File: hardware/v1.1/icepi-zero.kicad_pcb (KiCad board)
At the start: 4 copper layers, 65 x 30 mm, 144 parts, among them J1 Conn_02x20_Counter_Clockwise, J2 HDMI_C_1.3, J3 USB_C_Receptacle_USB2.0_14P, J4 USB_C_Receptacle_USB2.0_14P, J5 USB_C_Receptacle_USB2.0_14P, J6 Micro_SD_Card_Det2, SW1 SW_Push, SW2 SW_Push, U1 ECP5U_25F_CABGA256, U10 W9825G6KH, U11 W25Q128JVS, U2 TLV62569DBV, U3 TLV62569DBV, U4 TLV62569DBV, U5 PCA9306DC1, U6 FT231XQ, U7 TPD2EUSB30A, U8 TPD2EUSB30A, U9 TPD2EUSB30A, Y1 SITxxxxxx-1x-33E-50.000000

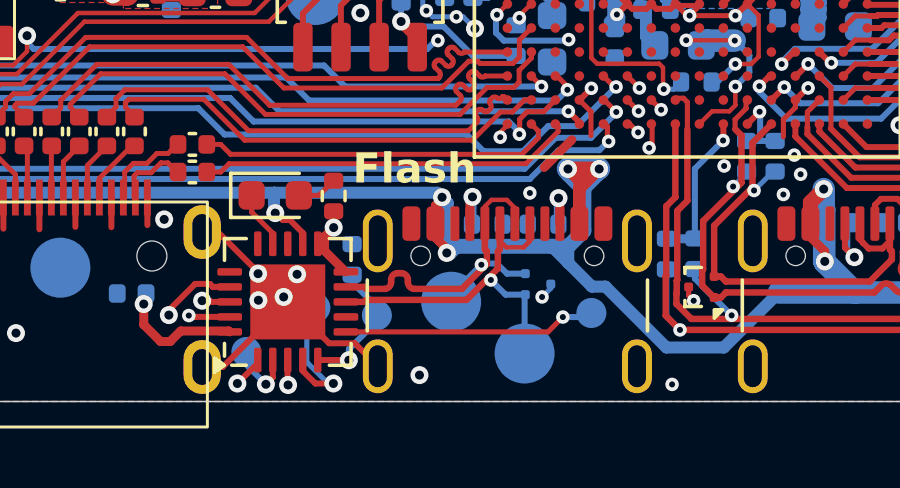
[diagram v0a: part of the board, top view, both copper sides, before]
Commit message: Fix wrong dates on shematic and pcb sheet
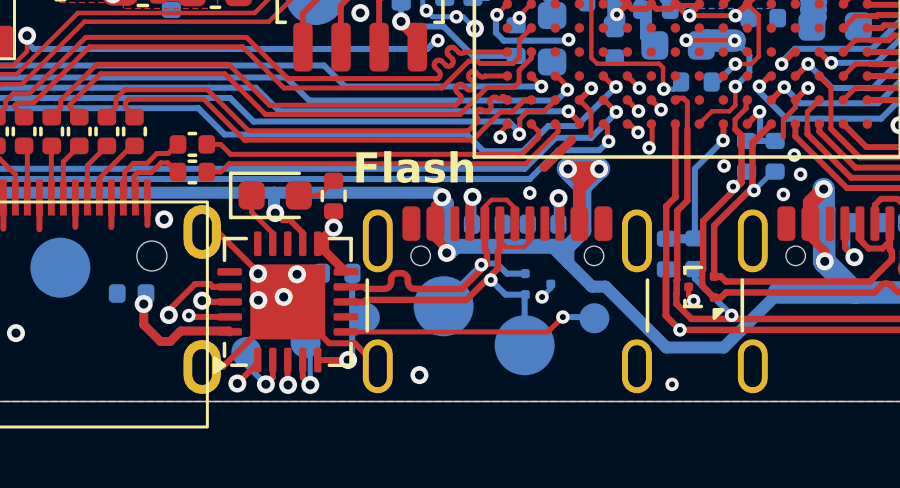
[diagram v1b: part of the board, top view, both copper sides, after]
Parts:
- moved TP9 1.22 mm to (137.3, 118.0)
- moved R25 0.68 mm to (138.3, 115.7), turned to 180 degrees
- moved TP12 0.41 mm to (139.2, 117.2)
- moved TP7 0.29 mm to (141.9, 116.8)
- moved TP8 0.28 mm to (144.6, 118.1)
- moved TP11 0.20 mm to (146.9, 117.2)
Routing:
- net JTAG_TCK: track 35.9 -> 33.9 mm

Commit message: Update pcb pic on readme
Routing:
- net GND: track 83.6 -> 89.4 mm
- net +5V: track 187.1 -> 185.6 mm
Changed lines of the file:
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@@
 	)
 	(segment
+		(start 146.786 111.378811)
+		(end 147.499999 112.09281)
+		(width 0.17)
+		(layer "F.Cu")
+		(net 38)
+	)
+	(segment
 		(start 130 100.25)
 		(end 129.54 100.71)
@@
 	)
 	(segment
+		(start 147.499999 112.09281)
+		(end 147.499999 113.770001)
+		(width 0.17)
+		(layer "F.Cu")
+		(net 38)
+	)
+	(segment
 		(start 135.803788 98.2425)
 		(end 135.3025 98.2425)
@@
 	)
 	(segment
+		(start 146.786 110.336)
+		(end 146.786 111.378811)
+		(width 0.17)
+		(layer "F.Cu")
+		(net 38)
+	)
+	(segment
 		(start 148.8 105.991141)
 		(end 149.208767 106.399908)
@@
 	)
 	(segment
+		(start 147.499999 113.770001)
+		(end 147.2 114.07)
+		(width 0.17)
+		(layer "F.Cu")
+		(net 38)
+	)
+	(segment
 		(start 150.4 110.75)
 		(end 150.824 110.326)
@@
 	)
 	(segment
+		(start 146.4 109.95)
+		(end 146.786 110.336)
+		(width 0.17)
+		(layer "F.Cu")
+		(net 38)
+	)
+	(segment
 		(start 149.92763 106.323234)
 		(end 149.950864 106.3)
@@
 	)
 	(segment
-		(start 146.786 110.336)
-		(end 146.786 111.139)
-		(width 0.17)
-		(layer "F.Cu")
-		(net 38)
-	)
-	(segment
 		(start 148.371717 103.979252)
 		(end 148.400001 103.950968)
@@
 	)
 	(segment
-		(start 146.4 109.95)
-		(end 146.786 110.336)
-		(width 0.17)
-		(layer "F.Cu")
-		(net 38)
-	)
-	(segment
 		(start 145.176 105.574)
 		(end 145.774 105.574)
@@
 	)
 	(segment
+		(start 141.1465 106.1735)
+		(end 139.9765 106.1735)
+		(width 0.165)
+		(layer "B.Cu")
+		(net 38)
+	)
+	(segment
 		(start 152.066 108.456)
 		(end 151.58 107.97)
@@
 	)
 	(segment
+		(start 139.9765 106.1735)
+		(end 139.1 107.05)
+		(width 0.165)
+		(layer "B.Cu")
+		(net 38)
+	)
+	(segment
 		(start 152.13 103.76)
 		(end 151.21 103.76)
@@
 	)
 	(segment
+		(start 141.18 106.14)
+		(end 141.1465 106.1735)
+		(width 0.165)
+		(layer "B.Cu")
+		(net 38)
+	)
+	(segment
 		(start 149.23 106.37)
 		(end 149.58 106.02)
@@
 	)
 	(segment
+		(start 146.85 112.46)
+		(end 146.4 112.91)
+		(width 0.4)
+		(layer "F.Cu")
+		(net 48)
+	)
+	(segment
 		(start 136.749581 99.675)
 		(end 136.731258 99.693323)
@@
 	)
 	(segment
+		(start 146.4 112.91)
+		(end 146.4 114.07)
+		(width 0.4)
+		(layer "F.Cu")
+		(net 48)
+	)
+	(segment
 		(start 131.85 100.2)
 		(end 131.97 100.2)
@@
 	)
 	(segment
-		(start 146.4 114.07)
-		(end 146.4 112.91)
-		(width 0.4)
-		(layer "F.Cu")
-		(net 48)
-	)
-	(segment
 		(start 171.4 114.608281)
 		(end 170.96 115.048281)
@@
 	)
 	(segment
+		(start 146.85 112.25)
+		(end 146.85 112.46)
+		(width 0.4)
+		(layer "F.Cu")
+		(net 48)
+	)
+	(segment
 		(start 128.59 100.562501)
 		(end 128.801251 100.351251)
@@
 	)
 	(segment
-		(start 146.02 112.25)
-		(end 147.06 112.25)
-		(width 0.5)
-		(layer "F.Cu")
-		(net 48)
-	)
-	(segment
 		(start 154.1 114.07)
 		(end 154.1 114.514682)
@@
 	)
 	(segment
-		(start 146.4 112.91)
-		(end 147.06 112.25)
-		(width 0.4)
-		(layer "F.Cu")
-		(net 48)
-	)
-	(segment
 		(start 129.954499 99.485501)
 		(end 129.667 99.485501)
@@
 	)
 	(via
-		(at 147.06 112.25)
+		(at 146.85 112.25)
 		(size 0.6)
 		(drill 0.3)
@@
 	)
 	(segment
+		(start 146.85 112.25)
+		(end 146.02 112.25)
+		(width 0.75)
+		(layer "B.Cu")
+		(net 48)
+	)
+	(segment
+		(start 146.85 112.25)
+		(end 146.85 112.48)
+		(width 0.75)
+		(layer "B.Cu")
+		(net 48)
+	)
+	(segment
 		(start 123.916447 111.383553)
 		(end 124.25 111.717106)
@@
 	)
 	(segment
-		(start 147.06 112.439)
-		(end 146.55 112.949)
-		(width 0.4)
+		(start 146.55 112.55)
+		(end 146.85 112.25)
+		(width 0.5)
 		(layer "B.Cu")
 		(net 48)
@@
 	(segment
 		(start 146.55 114.307618)
-		(end 146.55 112.949)
+		(end 146.55 113.2)
 		(width 0.5)
 		(layer "B.Cu")
@@
 	)
 	(segment
+		(start 146.85 112.48)
+		(end 146.55 112.78)
+		(width 0.75)
+		(layer "B.Cu")
+		(net 48)
+	)
+	(segment
 		(start 147.27 116.17)
 		(end 146.81757 116.17)
@@
 	)
 	(segment
+		(start 146.55 113.2)
+		(end 146.55 112.55)
+		(width 0.5)
+		(layer "B.Cu")
+		(net 48)
+	)
+	(segment
 		(start 142.061917 115.048083)
 		(end 142.283488 114.826512)
@@
 	)
 	(segment
-		(start 147.06 112.25)
-		(end 147.06 112.439)
-		(width 0.4)
-		(layer "B.Cu")
-		(net 48)
-	)
-	(segment
 		(start 154.58 115.33)
 		(end 154.561 115.311)
@@
 	)
 	(segment
-		(start 146.020001 112.24)
-		(end 147.051876 112.24)
-		(width 0.75)
-		(layer "B.Cu")
-		(net 48)
-	)
-	(segment
 		(start 146.564 112.314)
 		(end 146.625 112.375)
@@
 	)
 	(segment
+		(start 146.02 112.25)
+		(end 146.55 112.78)
+		(width 0.75)
+		(layer "B.Cu")
+		(net 48)
+	)
+	(segment
 		(start 135.573323 99.693323)
 		(end 137.076677 99.693323)
@@
 	)
 	(segment
-		(start 146.02 112.419)
-		(end 146.55 112.949)
-		(width 0.5)
-		(layer "B.Cu")
-		(net 48)
-	)
-	(segment
 		(start 136.23 113.04)
 		(end 141.6704 113.04)
@@
 	)
 	(segment
-		(start 147.051876 112.447124)
-		(end 146.55 112.949)
-		(width 0.3)
-		(layer "B.Cu")
-		(net 48)
-	)
-	(segment
 		(start 146.031106 115.383536)
 		(end 146.031106 114.826512)
@@
 	)
 	(segment
-		(start 146.02 112.189)
-		(end 146.02 112.419)
-		(width 0.5)
+		(start 117.975 112.65)
+		(end 124.25 112.65)
+		(width 0.75)
 		(layer "B.Cu")
 		(net 48)
 	)
 	(segment
-		(start 117.975 112.65)
-		(end 124.25 112.65)
-		(width 0.75)
+		(start 146.55 113.2)
+		(end 146.55 112.78)
+		(width 0.5)
 		(layer "B.Cu")
 		(net 48)
@@
 		(layer "B.Cu")
 		(net 48)
-	)
-	(segment
-		(start 147.051876 112.189001)
-		(end 147.051876 112.447124)
-		(width 0.3)
-		(layer "B.Cu")
-		(net 48)
